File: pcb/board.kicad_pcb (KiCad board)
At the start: 2 copper layers, 38 x 38 mm, 16 parts, among them J1 0473460001, J4 Conn_01x06_Male, Q1 Q_NMOS_GSD, Q2 Q_NMOS_GSD, U1 CP2102N-A01-GQFN28, U2 NUF2042XV6T1G

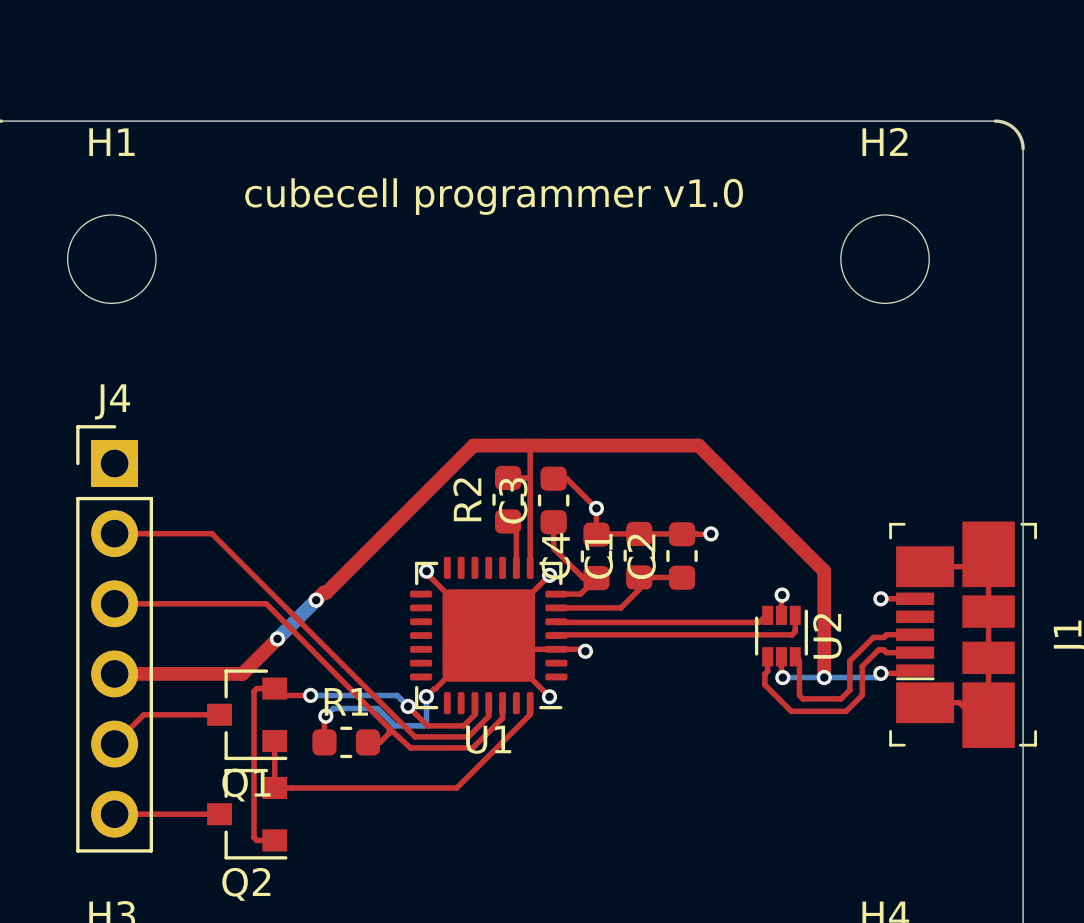
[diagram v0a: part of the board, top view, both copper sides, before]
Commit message: fixed missing 5v connection and changed ESD diodes
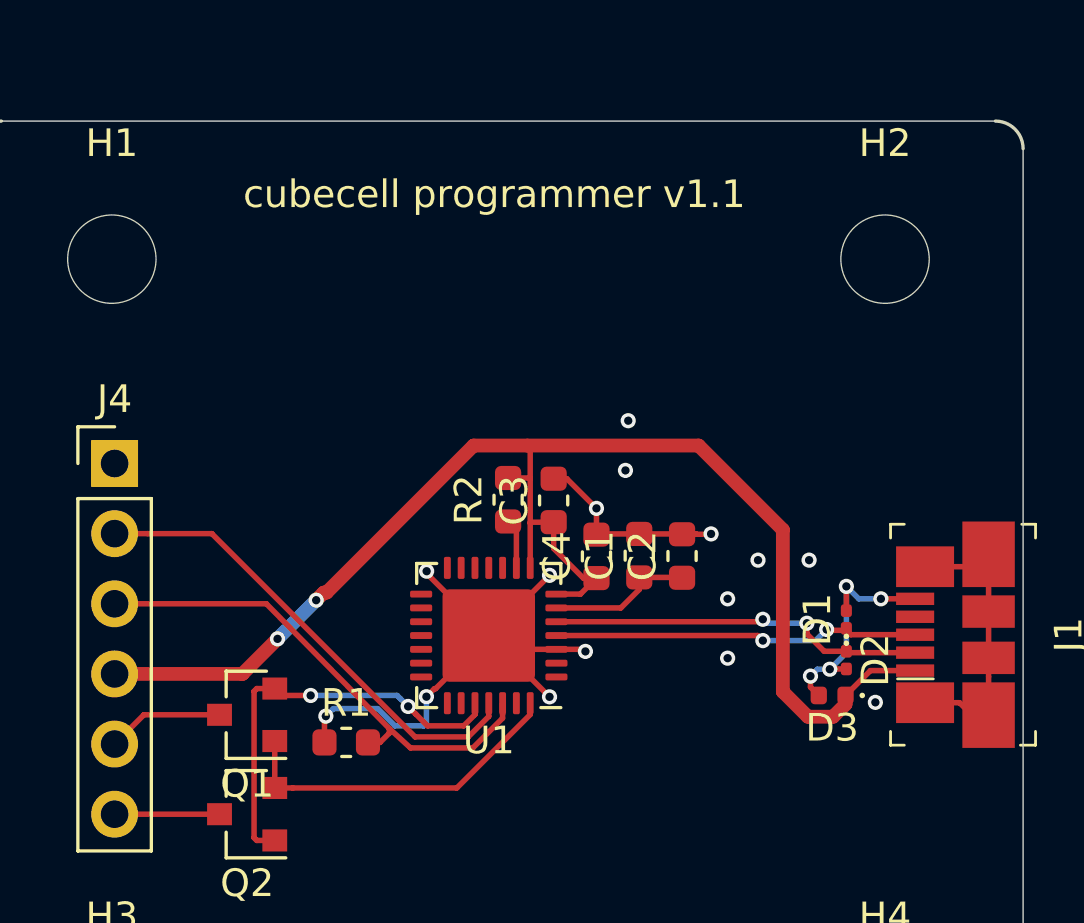
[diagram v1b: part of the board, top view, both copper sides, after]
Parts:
- removed U2: NUF2042XV6T1G, parts:SOT-563
- added D1: ESD7331MUT5G, Diode_SMD:D_0201_0603Metric, F.Cu at (142.6, 129.1)
- added D2: ESD7331MUT5G, Diode_SMD:D_0201_0603Metric, F.Cu at (142.6, 130.5)
- added D3: ESD9B5.0ST5G, Diode_SMD:D_0402_1005Metric, F.Cu at (142.1, 131.8)
- Q1, Q2: value Q_NMOS_GSD -> AO3400A
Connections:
- C3 pad 1: Net-(C3-Pad1) -> +5V
- C4 pad 1: Net-(C3-Pad1) -> +5V
- J1 pad 2: /ED- -> /D-
- J1 pad 3: /ED+ -> /D+
- U1 pad 7: Net-(C3-Pad1) -> +5V
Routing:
- net /ED-: track 8.47 -> 0.00 mm
- net /ED+: track 7.28 -> 0.00 mm
- net GND: track 32.5 -> 39.6 mm, vias 10 -> 19
- net /D-: track 7.77 -> 13.8 mm, vias 0 -> 2
- net +5V: track 45.8 -> 51.6 mm, vias 5 -> 2
- net Net-(C3-Pad1): track 4.64 -> 0.00 mm
- net /D+: track 9.30 -> 13.3 mm, vias 0 -> 2
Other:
- board text added: "cubecell programmer v1.1"
- board text removed: "cubecell programmer v1.0"
